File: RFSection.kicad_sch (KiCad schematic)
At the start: 5 parts, among them J2 Conn_Coaxial

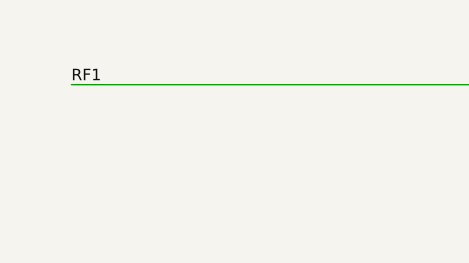
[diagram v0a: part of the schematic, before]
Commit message: fixed some nets
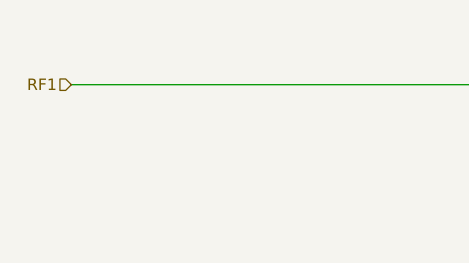
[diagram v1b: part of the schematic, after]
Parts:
- C14, C15: footprint (none) -> Capacitor_SMD:C_0402_1005Metric
- J2: footprint (none) -> Connector_Molex:Molex_PicoBlade_53048-0410_1x04_P1.25mm_Horizontal
- L3: footprint (none) -> Inductor_SMD:L_0402_1005Metric
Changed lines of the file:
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@@
 		)
 	)
-	(label "RF1"
-		(at 66.04 95.25 0)
+	(hierarchical_label "RF1"
+		(shape input)
+		(at 66.04 95.25 180)
 		(effects
 			(font
 				(size 1.27 1.27)
 			)
-			(justify left bottom)
+			(justify right)
 		)
 	)
@@
 			)
 		)
-		(property "Footprint" ""
+		(property "Footprint" "Capacitor_SMD:C_0402_1005Metric"
 			(at 121.6152 106.68 0)
 			(effects
@@
 			)
 		)
-		(property "Footprint" ""
+		(property "Footprint" "Connector_Molex:Molex_PicoBlade_53048-0410_1x04_P1.25mm_Horizontal"
 			(at 179.07 95.25 0)
 			(effects
@@
 			)
 		)
-		(property "Footprint" ""
+		(property "Footprint" "Inductor_SMD:L_0402_1005Metric"
 			(at 128.27 95.25 0)
 			(effects
@@
 			)
 		)
-		(property "Footprint" ""
+		(property "Footprint" "Capacitor_SMD:C_0402_1005Metric"
 			(at 138.1252 106.68 0)
 			(effects
